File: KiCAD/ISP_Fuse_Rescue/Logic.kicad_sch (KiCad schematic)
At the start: 6 parts, among them U1 74HCT4053N, U2 74HCT4053N

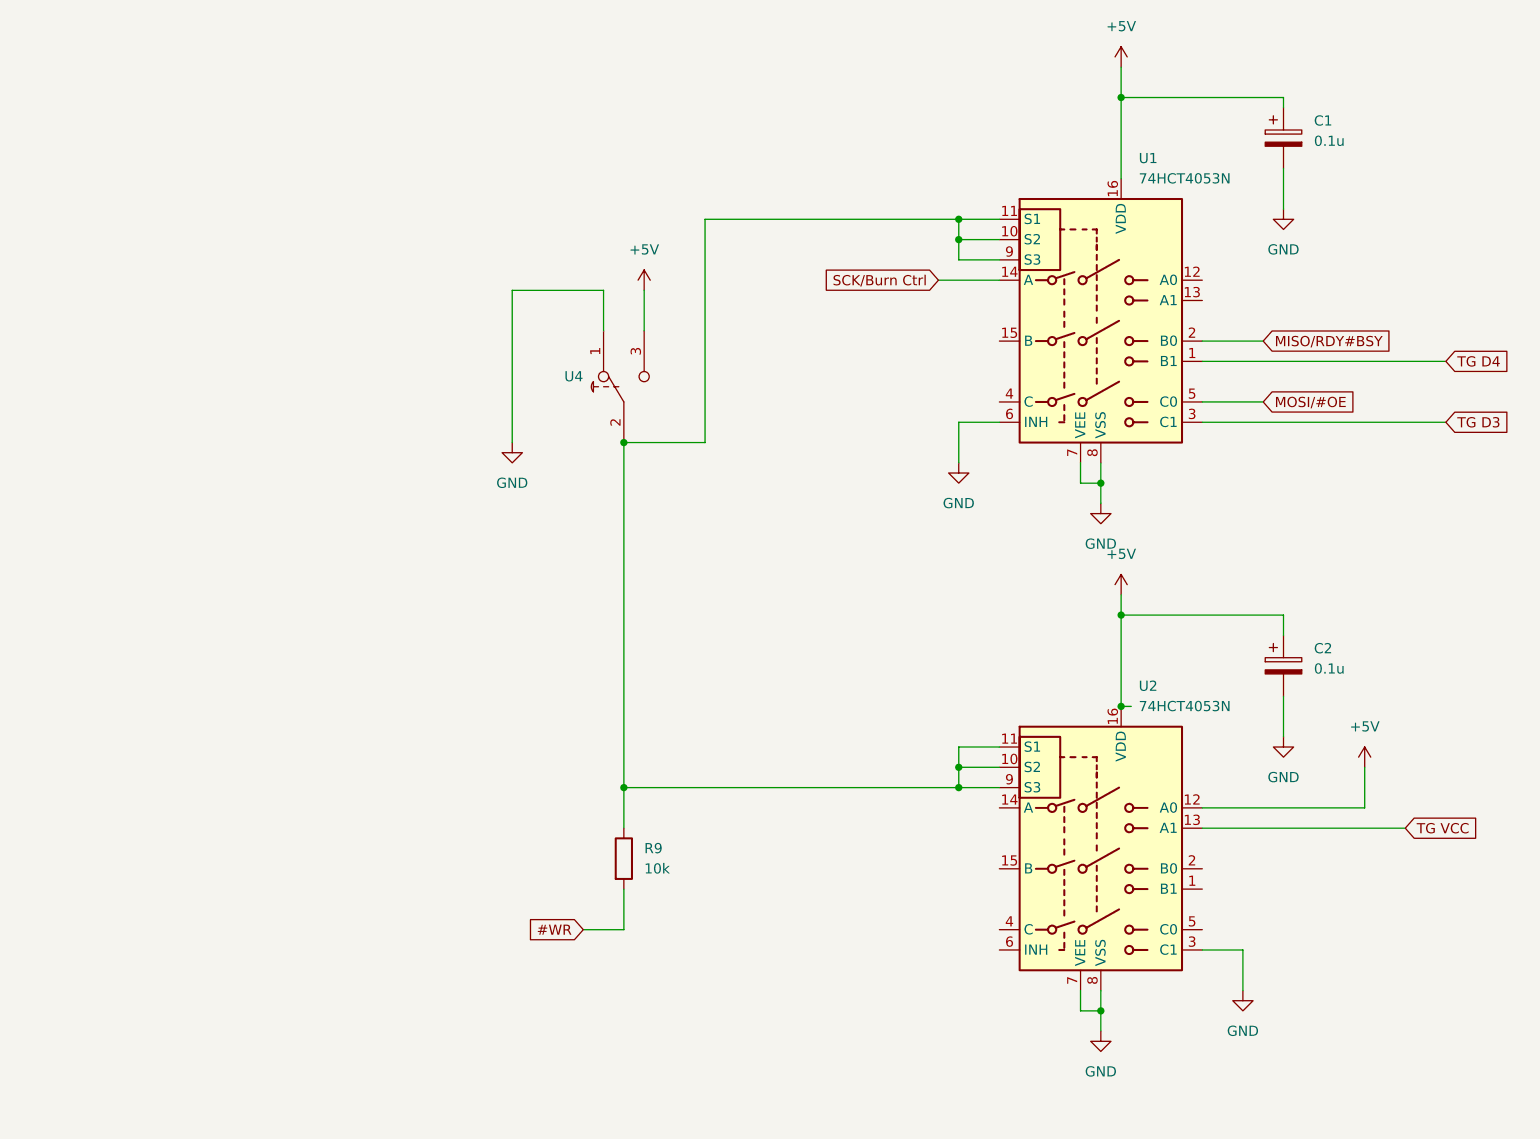
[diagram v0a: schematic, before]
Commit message: ISP Fuse Rescue
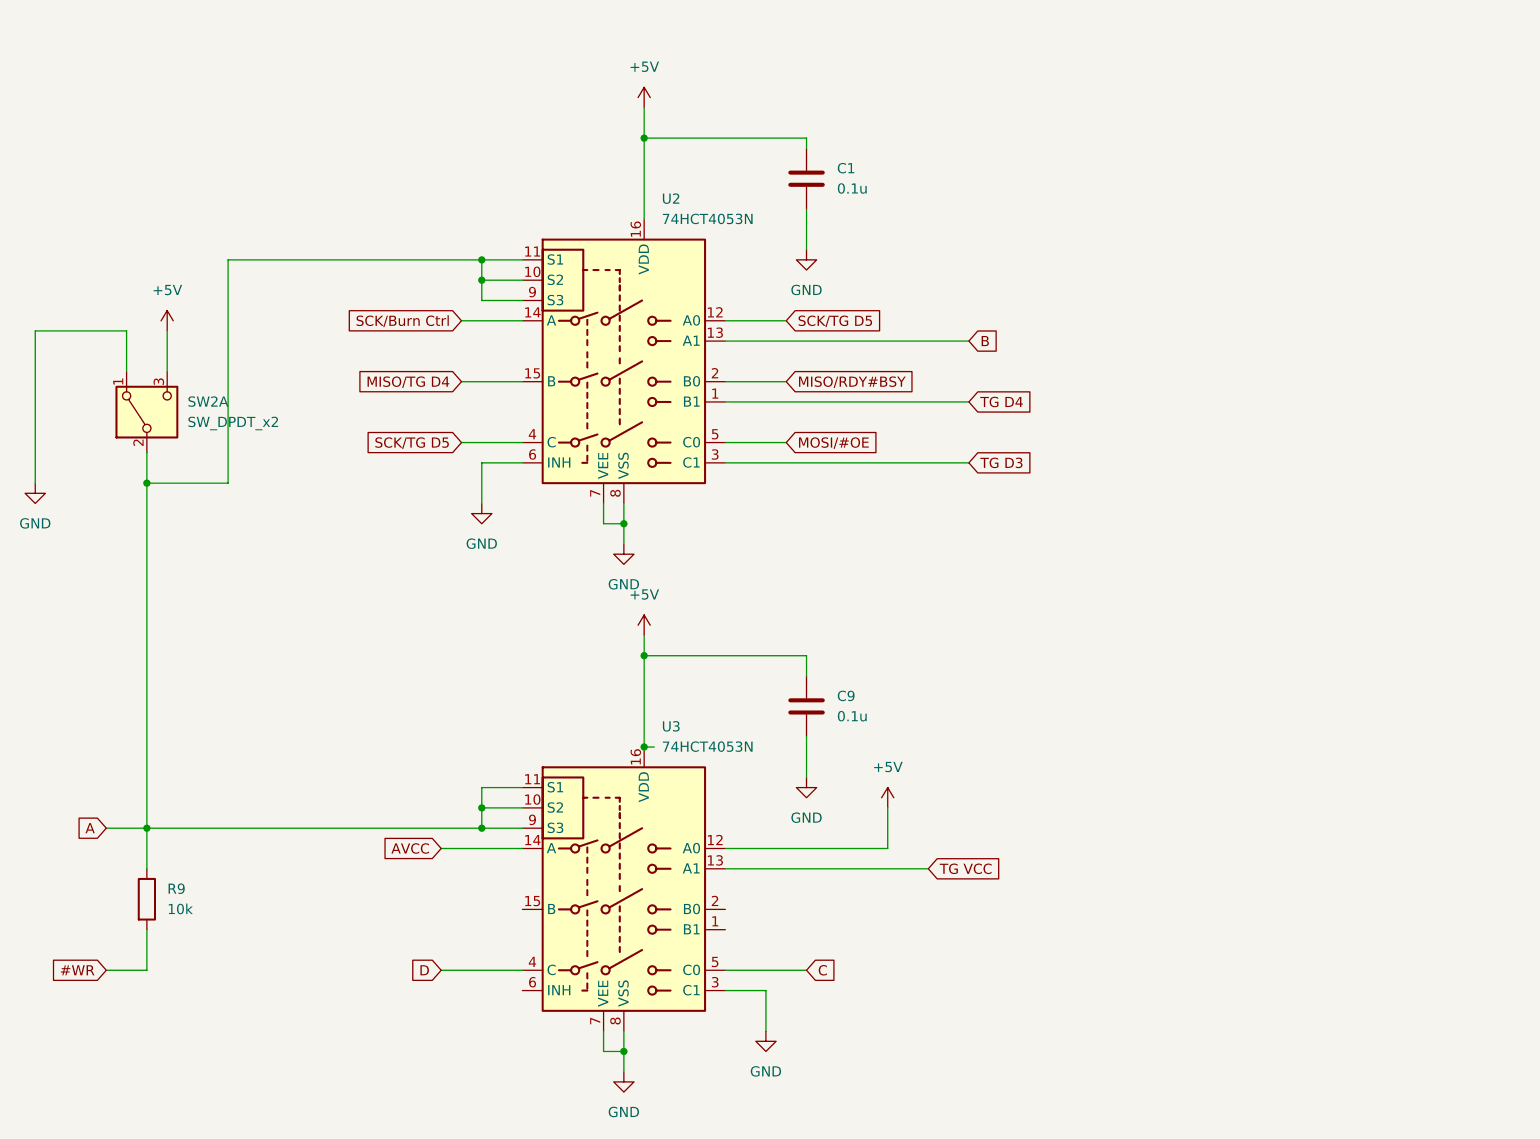
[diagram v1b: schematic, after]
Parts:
- removed C1, C2: 0.1u, symbol Device:C_Polarized
- removed U4: ~, symbol My_Parts:Toggling_Switch
- added C1, C9: 0.1u, My_Misc:C_Disc_D3.0mm_W1.6mm_P2.50mm_larg, symbol Device:C
- added SW2: SW_DPDT_x2, My_Parts:Switch sub-miniatyr 2-pole on-on, symbol Switch:SW_DPDT_x2
- R9: footprint (none) -> My_Misc:R_Axial_DIN0207_L6.3mm_D2.5mm_P10.16mm_Horizontal_large
- renumbered U1 to U2, U2 to U3
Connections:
- net +5V: now also C1.1, C9.1, SW2.3 (C)
- net GND: now also C1.2, C9.2, SW2.1 (A)
- net A: now reaches R9.1, U2.10 (S2), U2.11 (S1), U2.9 (S3), U3.10 (S2), U3.11 (S1), U3.9 (S3)
- net A: now also SW2.2 (B)
- net SCK/TG D5: now reaches U2.12 (A0)
- net SCK/TG D5: now also U2.4 (C)
- net B: now reaches U2.13 (A1)
- net MISO/TG D4: now reaches U2.15 (B)
- net AVCC: now reaches U3.14 (A)
- net D: now reaches U3.4 (C)
- net C: now reaches U3.5 (C0)
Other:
- moved on the sheet: R9, U2, U3
